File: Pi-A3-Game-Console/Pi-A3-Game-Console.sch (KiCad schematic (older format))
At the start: 42 parts, among them J1 Raspberry_Pi_2_3, J2 ILI9341-3.2\"-TFT-LCD-Module, J3 Right Joystick, J4 Left Joystick, J5 Power Input, J6 Link Cable Connector, J7 AVR-ISP-6, J8 USB_B_Mini, Q1 BSS138, Q2 BSS138, SW1 D_PAD_UP_Button, SW10 R_Button, SW11 START_Button, SW12 SELECT_Button, SW13 HOME_Button, SW14 AUDIO_MUTE, SW15 BACKLIGHT_Button, SW2 D_PAD_LEFT_Button, SW3 D_PAD_RIGHT_Button, SW4 D_PAD_DOWN_Button, SW5 A_Button, SW6 B_Button, SW7 X_Button, SW8 Y_Button, SW9 L_Button, U1 ATmega32U4-AU, U2 MAX98357A-Mono-3W-I2S, U3 BatteryShield, Y1 16Mhz

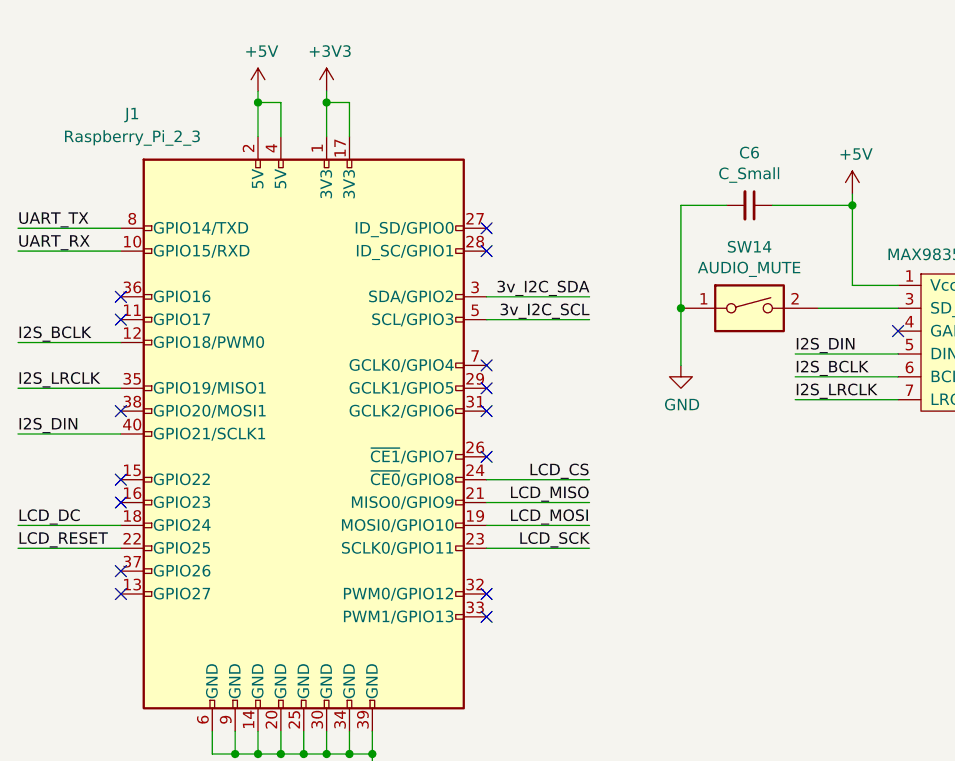
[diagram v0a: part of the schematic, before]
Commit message: Added the prototype 32u4 code.  Also PCB tweaks.
Mostly stuff related to mounting holes, though I've played around with the layout and a couple connections.  Overall I'm pretty happy with everything, feel like it's getting pretty close.
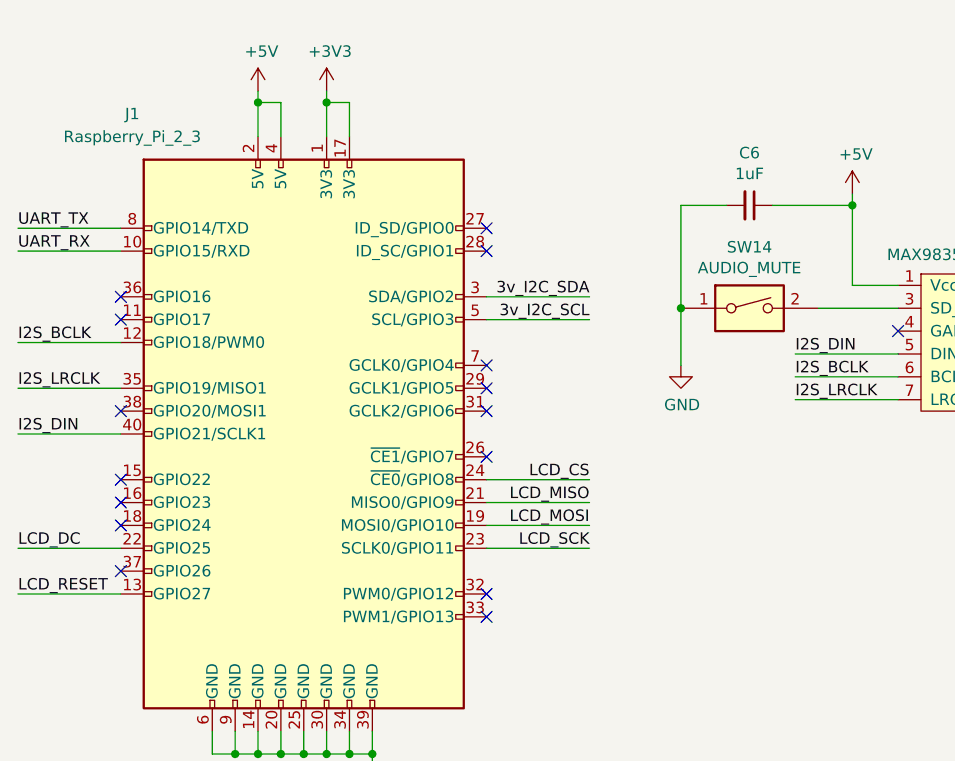
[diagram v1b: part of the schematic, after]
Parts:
- C6: value C_Small -> 1uF
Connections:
- net LCD_DC: now also J1.22 (GPIO25); no longer J1.18 (GPIO24)
- net LCD_RESET: now also J1.13 (GPIO27); no longer J1.22 (GPIO25)
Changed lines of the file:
@@
 Text Label 4250 3800 2    50   ~ 0
 LCD_CS
+Text Label 1750 4300 0    50   ~ 0
+LCD_RESET
 Text Label 1750 4100 0    50   ~ 0
-LCD_RESET
-Text Label 1750 4000 0    50   ~ 0
 LCD_DC
 Text Label 4250 4000 2    50   ~ 0
@@
 	4250 3800 3800 3800
 Wire Wire Line
+	1750 4300 2200 4300
+Wire Wire Line
 	1750 4100 2200 4100
-Wire Wire Line
-	1750 4000 2200 4000
 Wire Wire Line
 	4250 4000 3800 4000
@@
 P 4950 2600
 F 0 "C6" V 4721 2600 50  0000 C CNN
-F 1 "C_Small" V 4812 2600 50  0000 C CNN
+F 1 "1uF" V 4812 2600 50  0000 C CNN
 F 2 "Capacitor_SMD:C_1206_3216Metric_Pad1.42x1.75mm_HandSolder" H 4950 2600 50  0001 C CNN
 F 3 "~" H 4950 2600 50  0001 C CNN
@@
 NoConn ~ 2200 3000
 NoConn ~ 2200 3100
-NoConn ~ 2200 4300
+NoConn ~ 2200 4000
 NoConn ~ 2200 4200
 NoConn ~ 2200 3800

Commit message: bring repository up to speed again
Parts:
- SW15: value BACKLIGHT_Button -> MACRO_Button
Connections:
- net LCD_LED: now also J1.33 (PWM1/GPIO13); no longer J7.3 (SCK), U1.9 (PB1)
- net BACKLIGHT_BTN renamed MACRO_BTN
- new net MCU_SCLK: J7.3 (SCK), U1.9 (PB1)
- no-connect marks 22 -> 21
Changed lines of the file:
@@
 Text Label 13150 4200 2    50   ~ 0
 MCU_MOSI
-Text Label 13350 3700 3    50   ~ 0
+Text Label 13150 4100 2    50   ~ 0
 MCU_SCLK
 $Comp
@@
 Wire Wire Line
 	11800 3450 11800 3700
-Text Label 13150 4100 2    50   ~ 0
+Text Label 4250 4400 2    50   ~ 0
 LCD_LED
 $Comp
@@
 $EndComp
 Wire Wire Line
-	13350 4100 13350 3700
-Wire Wire Line
-	12500 4100 13350 4100
-Wire Wire Line
-	12500 6500 13150 6500
-Text Label 13150 6500 2    50   ~ 0
-BACKLIGHT_BTN
+	12500 4100 13150 4100
+Wire Wire Line
+	3800 4400 4250 4400
+Wire Wire Line
+	12500 6500 13100 6500
+Text Label 13100 6500 2    50   ~ 0
+MACRO_BTN
 $Comp
 L Switch:SW_Push SW15
@@
 P 14950 7850
 F 0 "SW15" H 14750 7950 50  0000 C CNN
-F 1 "BACKLIGHT_Button" H 14950 8050 50  0000 C CNN
+F 1 "MACRO_Button" H 14950 8050 50  0000 C CNN
 F 2 "Button_Switch_THT:SW_PUSH_6mm" H 14950 8050 50  0001 C CNN
 F 3 "~" H 14950 8050 50  0001 C CNN
@@
 	14750 7850 14150 7850
 Text Label 14150 7850 0    50   ~ 0
-BACKLIGHT_BTN
+MACRO_BTN
 $Comp
 L power:GND #PWR0136
@@
 NoConn ~ 3800 3700
 NoConn ~ 3800 4300
-NoConn ~ 3800 4400
 NoConn ~ 2200 3000
 NoConn ~ 2200 3100

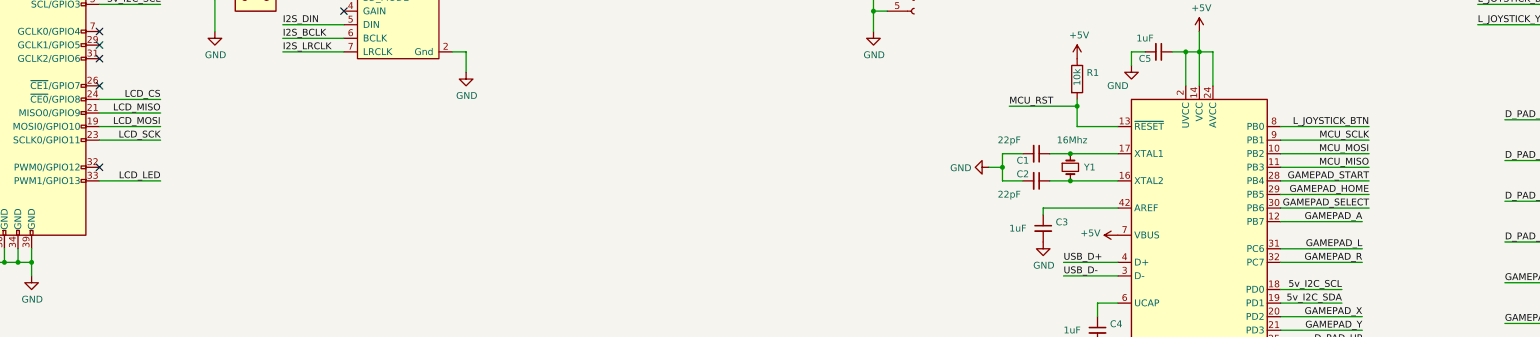
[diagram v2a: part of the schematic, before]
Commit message: update controller firmware
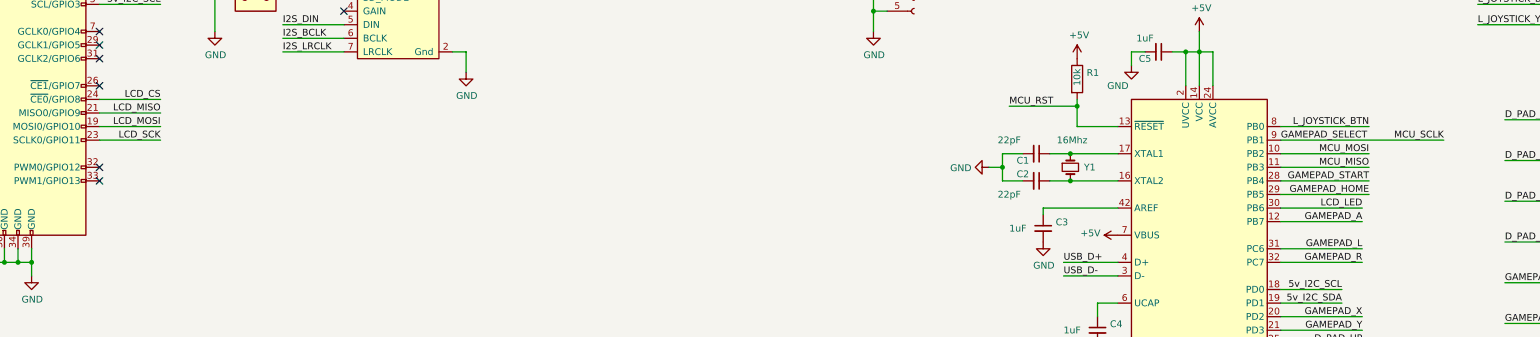
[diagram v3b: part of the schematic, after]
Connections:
- net MCU_SCLK is gone; now on net GAMEPAD_SELECT: J7.3 (SCK), U1.9 (PB1)
- net GAMEPAD_SELECT: no longer U1.30 (PB6)
- net LCD_LED: now also U1.30 (PB6); no longer J1.33 (PWM1/GPIO13)
- no-connect marks 21 -> 22
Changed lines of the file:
@@
 Text Label 13150 4400 2    50   ~ 0
 GAMEPAD_START
-Text Label 13150 4600 2    50   ~ 0
+Text Label 12500 4100 0    50   ~ 0
 GAMEPAD_SELECT
 Text Label 13150 4500 2    50   ~ 0
@@
 Wire Wire Line
 	12500 4400 13150 4400
-Wire Wire Line
-	12500 4600 13150 4600
 Wire Wire Line
 	12500 4500 13150 4500
@@
 Text Label 13150 4200 2    50   ~ 0
 MCU_MOSI
-Text Label 13150 4100 2    50   ~ 0
+Text Label 13700 4100 2    50   ~ 0
 MCU_SCLK
 $Comp
@@
 Wire Wire Line
 	11800 3450 11800 3700
-Text Label 4250 4400 2    50   ~ 0
-LCD_LED
 $Comp
 L MCU_Microchip_ATmega:ATmega32U4-AU U1
@@
 	1    0    0    -1
 $EndComp
-Wire Wire Line
-	12500 4100 13150 4100
-Wire Wire Line
-	3800 4400 4250 4400
 Wire Wire Line
 	12500 6500 13100 6500
@@
 	1    0    0    -1
 $EndComp
+Wire Wire Line
+	12500 4600 13100 4600
+Text Label 13100 4600 2    50   ~ 0
+LCD_LED
+NoConn ~ 3800 4400
+Wire Wire Line
+	12500 4100 13700 4100
 $EndSCHEMATC
